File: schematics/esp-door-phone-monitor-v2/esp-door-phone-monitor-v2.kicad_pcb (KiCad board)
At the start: 2 copper layers, 69.9 x 27.9 mm, 43 parts, among them J1 PHONE, J2 PWR_IN, J3 PROGRAM, K1 D3204, Q1 SS8050-G, Q2 SS8050-G, Q3 AO3480, U1 OP07, U2 AMS1117-3.3, U3 ESP-12E

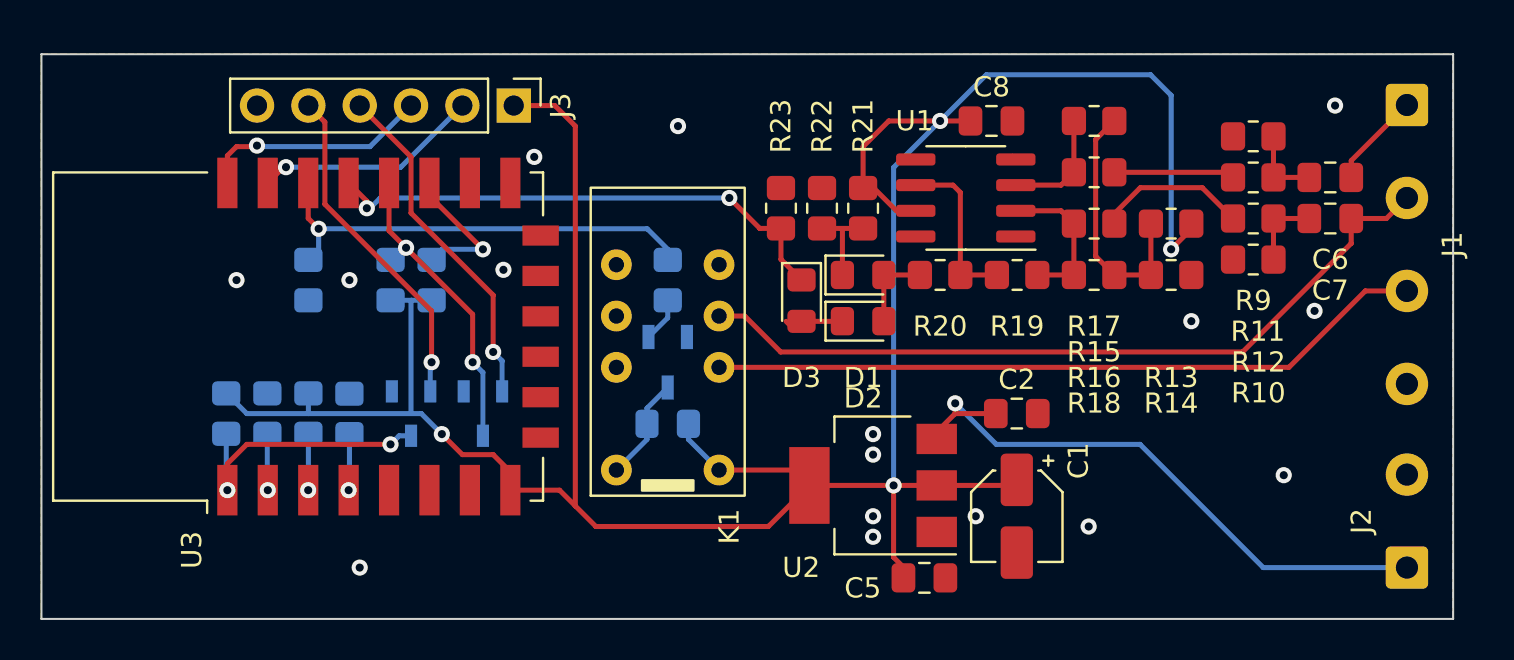
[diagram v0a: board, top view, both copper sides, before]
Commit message: New, more compact PCB design
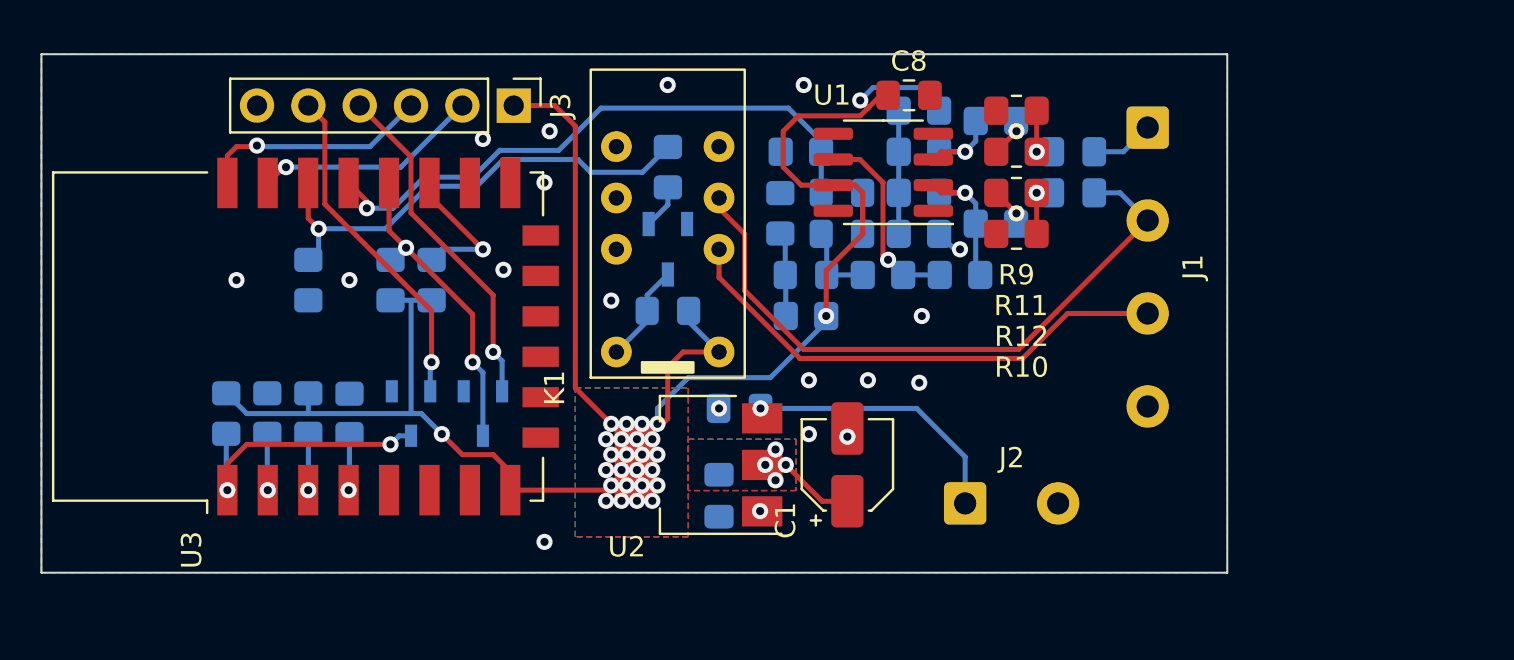
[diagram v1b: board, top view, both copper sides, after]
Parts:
- C2, C5, C6, C7, D1, D2, D3, R13, R14, R15, R16, R17, R18, R19, R20, R21, R22, R23: moved to B.Cu
- moved J2 22.1 mm to (153.9, 107.1), turned to 0 degrees
- moved C2 13.7 mm to (142.7, 102.4), turned to 180 degrees
- moved R13 13.7 mm to (151.6, 87.6)
- moved J1 12.9 mm to (162.9, 88.5)
- moved C6 12.8 mm to (159.3, 89.7)
- moved C7 12.8 mm to (159.3, 91.7)
- moved R14 12.6 mm to (151.6, 93.7)
- moved R10 11.8 mm to (156.4, 93.7)
- moved R11 11.8 mm to (156.4, 89.7)
- moved R12 11.8 mm to (156.4, 91.7)
- moved R9 11.8 mm to (156.4, 87.6)
- moved C5 10.9 mm to (141.7, 106.7), turned to -90 degrees
- moved R18 9.57 mm to (151.6, 91.7), turned to 0 degrees
- moved R17 8.80 mm to (151.6, 89.7), turned to 0 degrees
- moved C1 8.76 mm to (148.1, 105.2), turned to 90 degrees
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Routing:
- net VDD: track 139.0 -> 98.5 mm, vias 4 -> 31
- net +12V: track 29.9 -> 13.8 mm
- net SPEAKER_GND_OUT: track 35.6 -> 25.2 mm
- net Net-(R13-Pad2): track 13.0 -> 6.10 mm
- net SPEAKER_GND: track 38.7 -> 32.1 mm
- net Net-(R12-Pad2): track 8.07 -> 2.21 mm, vias 0 -> 1
- net Net-(R11-Pad2): track 5.98 -> 2.30 mm, vias 0 -> 1
- net ESP_RINGING_SENSE: track 25.9 -> 29.4 mm, vias 2 -> 1
- net SPEAKER_INPUT: track 4.73 -> 3.14 mm
- net Net-(R19-Pad2): track 8.25 -> 9.73 mm, vias 0 -> 1
- net Net-(C7-Pad2): track 4.07 -> 2.80 mm, vias 0 -> 1
- net ESP_MUTE_CTRL: track 22.4 -> 23.7 mm
- net GND: track 0.51 -> 1.58 mm, vias 16 -> 19
- net Net-(C6-Pad2): track 3.80 -> 2.80 mm, vias 0 -> 1
- net Net-(R16-Pad2): track 7.49 -> 8.16 mm, vias 0 -> 1
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- added copper zone on B.Cu, net VDD
- added copper zone on F.Cu, net VDD
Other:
- board size 69.9 x 27.9 mm -> 58.7 x 25.7 mm

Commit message: Even smaller PCB design
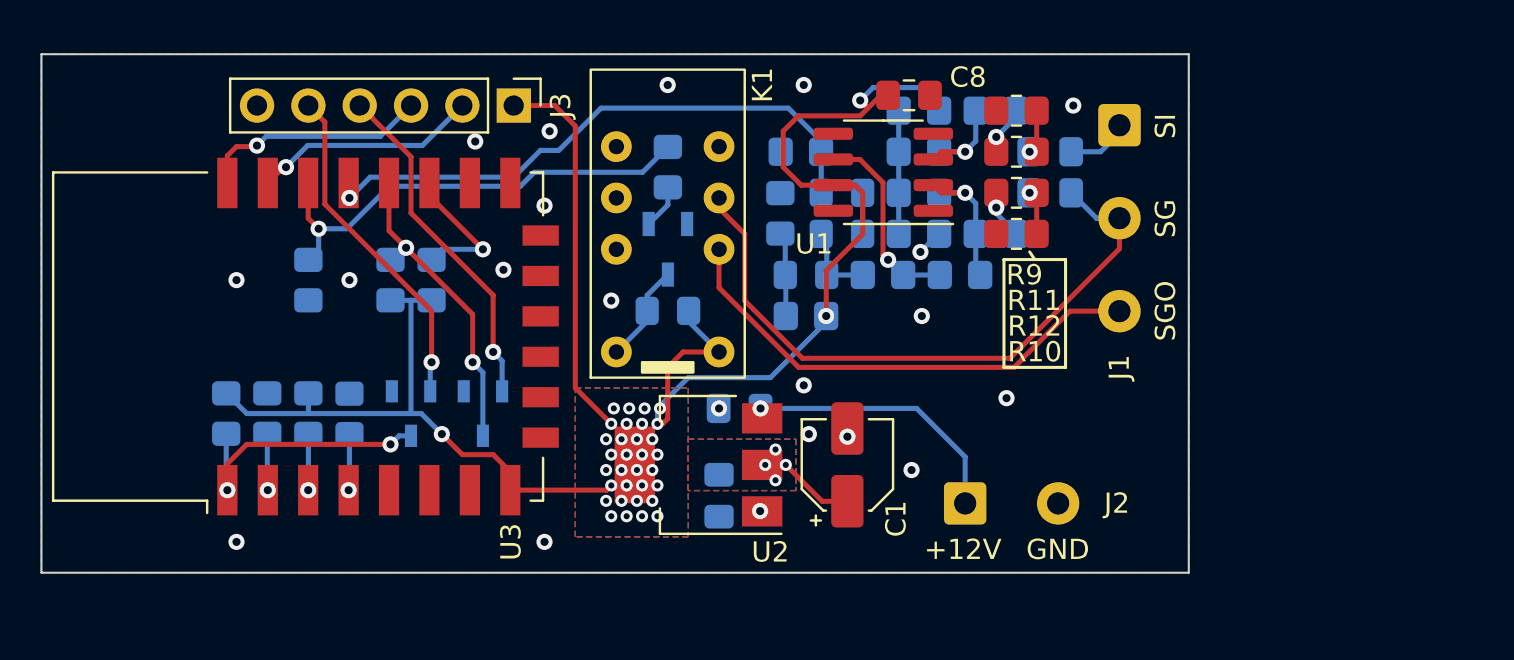
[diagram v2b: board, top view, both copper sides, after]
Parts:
- J1: footprint Connector_Wire:SolderWire-0.5sqmm_1x04_P4.6mm_D0.9mm_OD2.1mm -> Connector_Wire:SolderWire-0.5sqmm_1x03_P4.6mm_D0.9mm_OD2.1mm
- moved J1 1.40 mm to (161.5, 88.3)
- moved C6 1.14 mm to (158.1, 89.7)
- moved C7 1.14 mm to (158.1, 91.7)
- moved R15 0.51 mm to (155.4, 87.6)
- moved R16 0.51 mm to (155.4, 93.7)
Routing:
- net ESP_RINGING_SENSE: track 29.4 -> 28.4 mm
- net Net-(C7-Pad2): track 2.80 -> 2.05 mm
- net Net-(C6-Pad2): track 2.80 -> 2.05 mm
- net ESP_MUTE_CTRL: track 23.7 -> 23.2 mm
- net GND: track 1.58 -> 1.53 mm, vias 19 -> 21
- net VDD: vias 31 -> 39
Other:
- board size 58.7 x 25.7 mm -> 56.8 x 25.7 mm
- board text added: "+12V"
- board text added: "GND"
- board text added: "SG"
- board text added: "SGO"
- board text added: "SI"

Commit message: Fix PCB issues
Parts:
- added C3: 100n, Capacitor_SMD:C_0805_2012Metric_Pad1.18x1.45mm_HandSolder, B.Cu at (130.3, 106.4)
- added C4: 100n, Capacitor_SMD:C_0805_2012Metric_Pad1.18x1.45mm_HandSolder, B.Cu at (117.3, 98.8)
- added R1: 10k, Resistor_SMD:R_0805_2012Metric_Pad1.20x1.40mm_HandSolder, B.Cu at (126.5, 98.9)
- added R2: 10k, Resistor_SMD:R_0805_2012Metric_Pad1.20x1.40mm_HandSolder, B.Cu at (129.5, 98.8)
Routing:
- net PGM_RTS: track 16.7 -> 30.6 mm, vias 1 -> 2
- net VDD: track 98.5 -> 92.8 mm, vias 39 -> 43
- net ESP_~{RST}: track 13.8 -> 18.7 mm, vias 2 -> 3
- net PGM_DTR: track 17.1 -> 20.8 mm
- net Net-(Q1-Pad1): track 0.00 -> 2.65 mm
- net Net-(Q2-Pad1): track 0.00 -> 1.89 mm
- net Net-(R15-Pad2): track 5.60 -> 4.76 mm
- net Net-(R16-Pad2): track 8.16 -> 7.39 mm
- net GND: track 1.53 -> 1.30 mm, vias 21 -> 25

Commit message: Prepare PCB for manufacturing
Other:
- board text added: "ESP Door Phone Monitor (C) 2022 - tomikaa87 v1.0"
- board text added: "JLCJLCJLCJLC"
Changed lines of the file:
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@@
       (layerselection 0x00010fc_ffffffff)
       (disableapertmacros false)
-      (usegerberextensions false)
+      (usegerberextensions true)
       (usegerberattributes true)
       (usegerberadvancedattributes true)
@@
       (plotinvisibletext false)
       (sketchpadsonfab false)
-      (subtractmaskfromsilk false)
+      (subtractmaskfromsilk true)
       (outputformat 1)
       (mirror false)
@@
     (fp_circle (center 4.6 0) (end 5.65 0) (layer "F.Fab") (width 0.1) (fill none))
     (fp_circle (center 9.2 0) (end 10.25 0) (layer "F.Fab") (width 0.1) (fill none))
-    (pad "1" thru_hole roundrect locked (at 0 0 270) (size 2.1 2.1) (drill 1.1) (layers *.Cu *.Mask) (roundrect_rratio 0.119048)
+    (pad "1" thru_hole roundrect locked (at 0 0 270) (size 2.1 2.1) (drill 1.1) (layers *.Cu *.Mask) (roundrect_rratio 0.1190480952)
       (net 4 "SPEAKER_INPUT") (pinfunction "Pin_1") (pintype "passive"))
     (pad "2" thru_hole circle locked (at 4.6 0 270) (size 2.1 2.1) (drill 1.1) (layers *.Cu *.Mask)
@@
     (fp_line (start -1 0.625) (end 1 0.625) (layer "B.Fab") (width 0.1))
     (fp_line (start -1 -0.625) (end -1 0.625) (layer "B.Fab") (width 0.1))
-    (pad "1" smd roundrect locked (at -1 0 90) (size 1.2 1.4) (layers "B.Cu" "B.Paste" "B.Mask") (roundrect_rratio 0.208333)
+    (pad "1" smd roundrect locked (at -1 0 90) (size 1.2 1.4) (layers "B.Cu" "B.Paste" "B.Mask") (roundrect_rratio 0.2083333333)
       (net 28 "Net-(Q2-Pad1)") (pintype "passive"))
-    (pad "2" smd roundrect locked (at 1 0 90) (size 1.2 1.4) (layers "B.Cu" "B.Paste" "B.Mask") (roundrect_rratio 0.208333)
+    (pad "2" smd roundrect locked (at 1 0 90) (size 1.2 1.4) (layers "B.Cu" "B.Paste" "B.Mask") (roundrect_rratio 0.2083333333)
       (net 26 "PGM_RTS") (pintype "passive"))
     (model "${KICAD6_3DMODEL_DIR}/Resistor_SMD.3dshapes/R_0805_2012Metric.wrl"
@@
     (fp_line (start 1 -0.625) (end -1 -0.625) (layer "B.Fab") (width 0.1))
     (fp_line (start 1 0.625) (end 1 -0.625) (layer "B.Fab") (width 0.1))
-    (pad "1" smd roundrect locked (at -1 0) (size 1.2 1.4) (layers "B.Cu" "B.Paste" "B.Mask") (roundrect_rratio 0.208333)
+    (pad "1" smd roundrect locked (at -1 0) (size 1.2 1.4) (layers "B.Cu" "B.Paste" "B.Mask") (roundrect_rratio 0.2083333333)
       (net 6 "Net-(Q1-Pad1)") (pintype "passive"))
-    (pad "2" smd roundrect locked (at 1 0) (size 1.2 1.4) (layers "B.Cu" "B.Paste" "B.Mask") (roundrect_rratio 0.208333)
+    (pad "2" smd roundrect locked (at 1 0) (size 1.2 1.4) (layers "B.Cu" "B.Paste" "B.Mask") (roundrect_rratio 0.2083333333)
       (net 29 "PGM_DTR") (pintype "passive"))
     (model "${KICAD6_3DMODEL_DIR}/Resistor_SMD.3dshapes/R_0805_2012Metric.wrl"
@@
     (fp_line (start 1 0.625) (end 1 -0.625) (layer "B.Fab") (width 0.1))
     (fp_line (start 1 -0.625) (end -1 -0.625) (layer "B.Fab") (width 0.1))
-    (pad "1" smd roundrect locked (at -1.0375 0 90) (size 1.175 1.45) (layers "B.Cu" "B.Paste" "B.Mask") (roundrect_rratio 0.212766)
+    (pad "1" smd roundrect locked (at -1.0375 0 90) (size 1.175 1.45) (layers "B.Cu" "B.Paste" "B.Mask") (roundrect_rratio 0.2127659574)
       (net 27 "ESP_~{RST}") (pintype "passive"))
-    (pad "2" smd roundrect locked (at 1.0375 0 90) (size 1.175 1.45) (layers "B.Cu" "B.Paste" "B.Mask") (roundrect_rratio 0.212766)
+    (pad "2" smd roundrect locked (at 1.0375 0 90) (size 1.175 1.45) (layers "B.Cu" "B.Paste" "B.Mask") (roundrect_rratio 0.2127659574)
       (net 2 "GND") (pintype "passive"))
     (model "${KICAD6_3DMODEL_DIR}/Capacitor_SMD.3dshapes/C_0805_2012Metric.wrl"
@@
     (fp_line (start -1 0.625) (end 1 0.625) (layer "B.Fab") (width 0.1))
     (fp_line (start -1 -0.625) (end -1 0.625) (layer "B.Fab") (width 0.1))
-    (pad "1" smd roundrect locked (at -1.0375 0 180) (size 1.175 1.45) (layers "B.Cu" "B.Paste" "B.Mask") (roundrect_rratio 0.212766)
+    (pad "1" smd roundrect locked (at -1.0375 0 180) (size 1.175 1.45) (layers "B.Cu" "B.Paste" "B.Mask") (roundrect_rratio 0.2127659574)
       (net 1 "VDD") (pintype "passive"))
-    (pad "2" smd roundrect locked (at 1.0375 0 180) (size 1.175 1.45) (layers "B.Cu" "B.Paste" "B.Mask") (roundrect_rratio 0.212766)
+    (pad "2" smd roundrect locked (at 1.0375 0 180) (size 1.175 1.45) (layers "B.Cu" "B.Paste" "B.Mask") (roundrect_rratio 0.2127659574)
       (net 2 "GND") (pintype "passive"))
     (model "${KICAD6_3DMODEL_DIR}/Capacitor_SMD.3dshapes/C_0805_2012Metric.wrl"
@@
   (gr_line (start 157.353 94.996) (end 157.099 94.615) (layer "F.SilkS") (width 0.15))
   (gr_rect (start 108.204 84.836) (end 164.973 110.49) (layer "Edge.Cuts") (width 0.1) (fill none))
+  (gr_text "JLCJLCJLCJLC" (at 114.808 97.536 90) (layer "B.SilkS")
+    (effects (font (size 1 1) (thickness 0.15)) (justify mirror))
+  )
+  (gr_text "ESP Door Phone Monitor\n(C) 2022 - tomikaa87\nv1.0" (at 111.506 97.536 90) (layer "B.SilkS")
+    (effects (font (size 1 1) (thickness 0.15)) (justify mirror))
+  )
   (gr_text "SGO" (at 163.83 97.536 90) (layer "F.SilkS")
     (effects (font (size 1 1) (thickness 0.15)))
